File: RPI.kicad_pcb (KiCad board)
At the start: 2 copper layers, 65 x 56 mm, 35 parts, among them J1 Conn_01x02_Male, J2 GPIO, J5 Conn_01x06, J6 Conn_01x04, J7 Conn_01x03, J8 Conn_01x02, J9 Conn_01x02, Q1 IRF9540N, Q2 IRF9540N, Q3 BC856BDW1, SW1 SW_SPDT, SW2 SW_SPDT, U1 LM1085-ADJ

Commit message: Finalised for a check-up
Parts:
- added G***: LOGO, LOGO, F.Cu at (105.3, 85.7)

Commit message: Gerber files generated?
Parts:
- renumbered G*** to G
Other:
- board text removed: "F1"
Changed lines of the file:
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@@
   (net 6 "Net-(D2-Pad1)")
   (net 7 "VD")
-  (net 8 "Net-(J1-Pad2)")
+  (net 8 "Net-(F1-Pad1)")
   (net 9 "/GPIO2{slash}SDA1")
   (net 10 "/GPIO3{slash}SCL1")
@@
     (at 124 96.185263)
     (attr board_only exclude_from_pos_files exclude_from_bom)
-    (fp_text reference "G***" (at 2.182281 1.899801) (layer "F.SilkS")
+    (fp_text reference "G" (at 2.182281 2.814737) (layer "F.SilkS") hide
       (effects (font (size 0.3 0.3) (thickness 0.01)))
     )
@@
       (effects (font (size 1 1) (thickness 0.15)))
     )
-    (fp_text value "10u" (at 1.233747 1.783092 180) (layer "F.Fab")
+    (fp_text value "10u" (at 1.25 -3.516722 180) (layer "F.Fab")
       (effects (font (size 1 1) (thickness 0.15)))
     )
@@
     (property "Value_1" "MCCQ-122")
     (attr through_hole)
-    (fp_text reference "F1" (at 5.7 0.4 90) (layer "F.SilkS")
-      (effects (font (size 1.27 1.27) (thickness 0.254)))
+    (fp_text reference "F1" (at -2.833513 -0.019887 180) (layer "F.SilkS")
+      (effects (font (size 1 1) (thickness 0.15)))
     )
     (fp_text value "MCCQ-122" (at 5.7 0.4 90) (layer "F.SilkS") hide
       (effects (font (size 1.27 1.27) (thickness 0.254)))
     )
-    (fp_text user "${REFERENCE}" (at 5.7 0.4 90) (layer "F.Fab")
+    (fp_text user "${REFERENCE}" (at -2.618494 1.918593 180) (layer "F.Fab")
       (effects (font (size 1.27 1.27) (thickness 0.254)))
     )
@@
     (fp_line (start -1.65 -2) (end 13.05 -2) (layer "F.Fab") (width 0.2))
     (pad "1" thru_hole circle locked (at 0 0 270) (size 3.5 3.5) (drill 2.5239) (layers *.Cu *.Mask)
-      (net 8 "Net-(J1-Pad2)") (pinfunction "1") (pintype "passive"))
+      (net 8 "Net-(F1-Pad1)") (pinfunction "1") (pintype "passive"))
     (pad "2" thru_hole circle locked (at 3.7 0 270) (size 3.5 3.5) (drill 2.5239) (layers *.Cu *.Mask)
-      (net 8 "Net-(J1-Pad2)") (pinfunction "2") (pintype "passive"))
+      (net 8 "Net-(F1-Pad1)") (pinfunction "2") (pintype "passive"))
     (pad "3" thru_hole circle locked (at 7.7 0 270) (size 3.5 3.5) (drill 2.5239) (layers *.Cu *.Mask)
       (net 47 "Net-(F1-Pad3)") (pinfunction "3") (pintype "passive"))
@@
     (at 105.348613 85.695667)
     (attr board_only exclude_from_pos_files exclude_from_bom)
-    (fp_text reference "G***" (at 16.235225 12.411091) (layer "F.SilkS")
+    (fp_text reference "G" (at 0.258943 5.65) (layer "F.SilkS") hide
       (effects (font (size 0.4 0.4) (thickness 0.05)))
     )
@@
       (net 1 "GND") (pinfunction "Pin_1") (pintype "passive"))
     (pad "2" thru_hole circle (at -5 0 90) (size 3.5 3.5) (drill 1.9) (layers *.Cu *.Mask)
-      (net 8 "Net-(J1-Pad2)") (pinfunction "Pin_2") (pintype "passive"))
+      (net 8 "Net-(F1-Pad1)") (pinfunction "Pin_2") (pintype "passive"))
     (model "${KICAD6_3DMODEL_DIR}/Connector_AMASS.3dshapes/AMASS_XT30PW-M_1x02_P2.50mm_Horizontal.wrl"
       (offset (xyz 0 0 0))
@@
     (at 153.826708 61.588613)
     (attr board_only exclude_from_pos_files exclude_from_bom)
-    (fp_text reference "G***" (at -1.194086 2.150782) (layer "F.SilkS")
+    (fp_text reference "G" (at -1.826708 0.411387) (layer "F.SilkS") hide
       (effects (font (size 0.5 0.5) (thickness 0.1)))
     )
@@
     (effects (font (size 0.4 0.4) (thickness 0.08)))
   )
-  (gr_text "F1" (at 124.107573 76.340246) (layer "F.SilkS")
-    (effects (font (size 1 1) (thickness 0.15)))
-  )
   (gr_text "Motor Control" (at 159.915242 65.995222 90) (layer "F.SilkS")

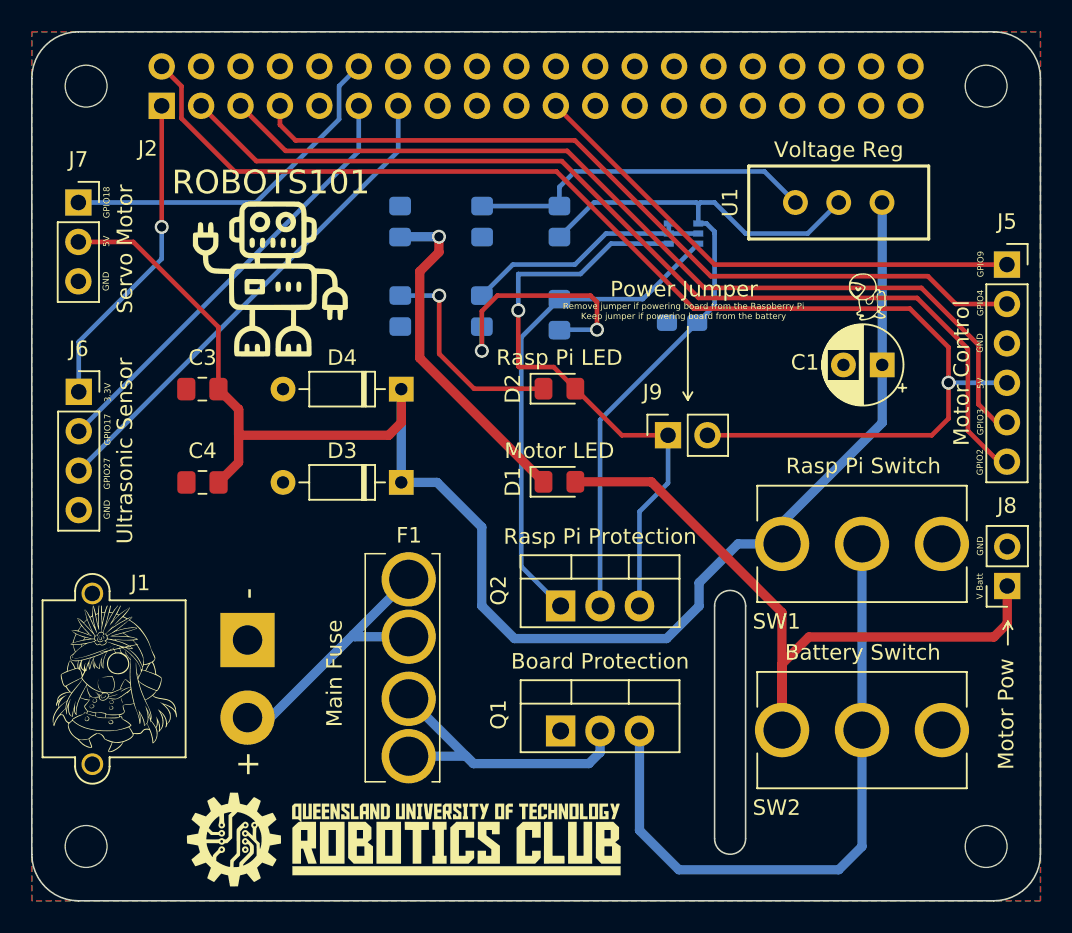
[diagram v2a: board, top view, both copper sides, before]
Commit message: fixed up using Fab ruleset and Matt's input
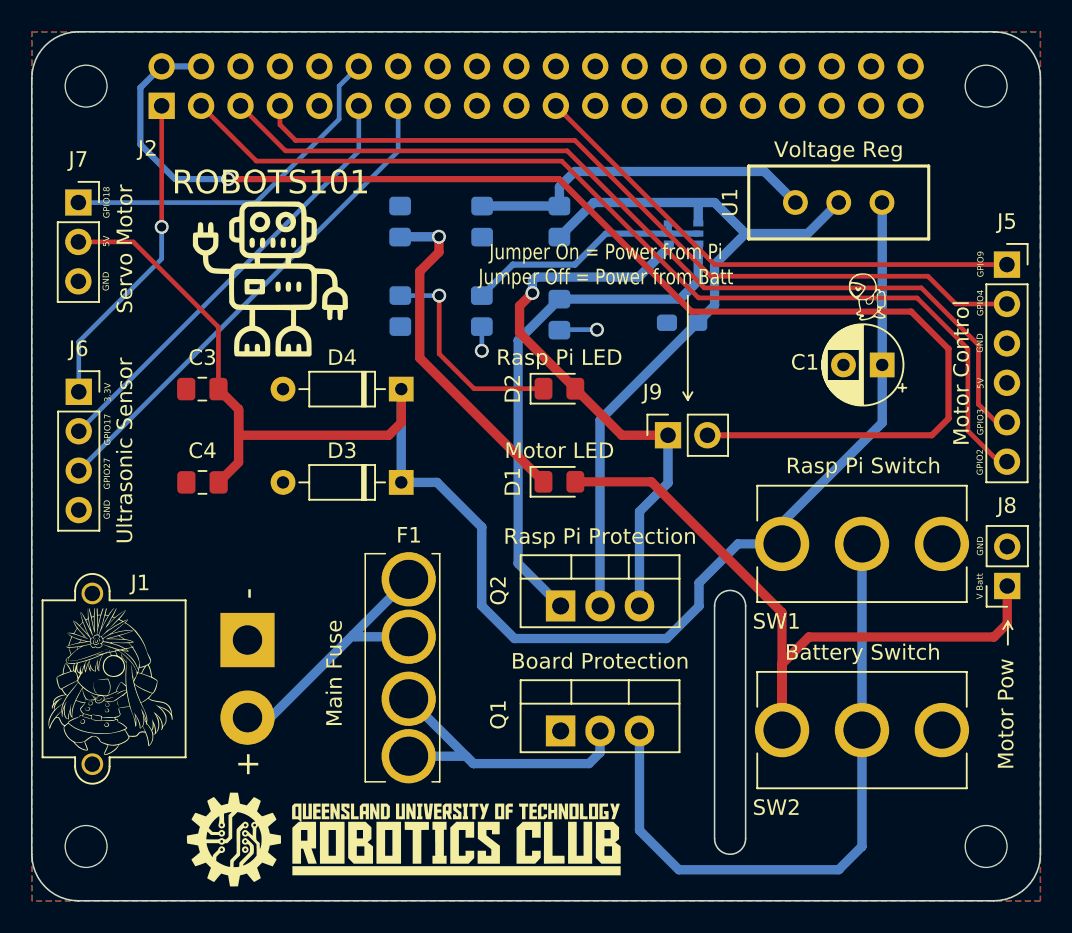
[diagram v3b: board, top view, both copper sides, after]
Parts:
- moved G 0.32 mm to (105.1, 85.9)
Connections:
- J2 pad 4: /5v -> +5V
- J5 pad 4: +5V -> unconnected-(J5-Pad4)
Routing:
- net GND: track 16.3 -> 3.99 mm
- net +5V: track 83.8 -> 86.1 mm
- net VD: track 39.7 -> 37.5 mm
- net Net-(Q2-Pad1): track 32.3 -> 33.6 mm
- net VDDA: track 50.3 -> 49.6 mm
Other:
- board text added: "Jumper On = Power from Pi Jumper Off = Power from Batt"
- board text removed: "Power Jumper"
- board text removed: "Remove jumper if powering board from the Raspberry Pi Keep jumper if powering board from the battery"

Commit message: Added load resistor & updated footprints
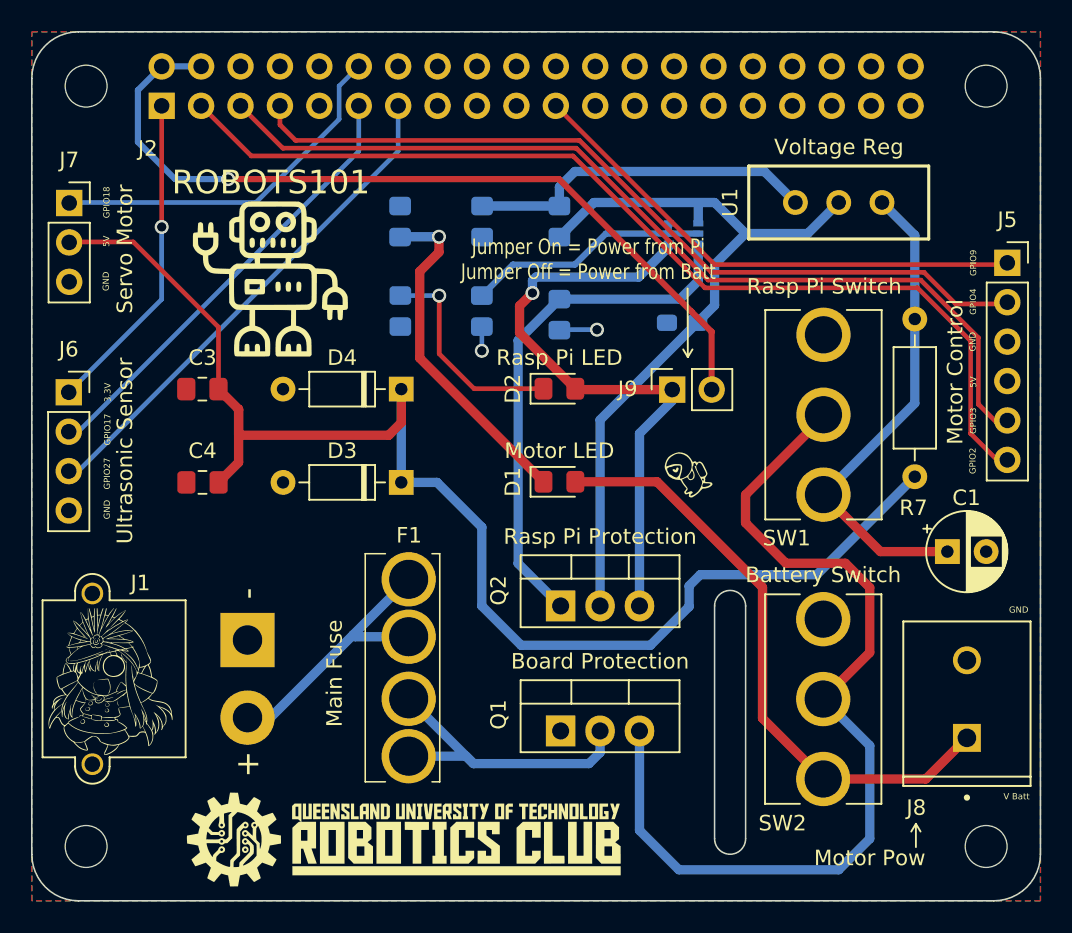
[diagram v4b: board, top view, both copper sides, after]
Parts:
- added R7: 3.3, Resistor_THT:R_Axial_DIN0207_L6.3mm_D2.5mm_P10.16mm_Horizontal, F.Cu at (156.9, 62.5)
- J8: footprint Connector_PinSocket_2.54mm:PinSocket_1x02_P2.54mm_Vertical -> RPi_Hat:TE_282836-2
- moved G 16.1 mm to (142.4, 72.9), turned to 25 degrees
- moved C1 12.7 mm to (159.0, 77.5), turned to 0 degrees
- moved SW1 8.69 mm to (151.0, 68.7), turned to 90 degrees
- moved J8 7.73 mm to (160.3, 87.0), turned to 90 degrees
- moved SW2 3.20 mm to (151.0, 87.0), turned to 90 degrees
- moved J9 2.96 mm to (141.3, 67.1)
- moved J6 0.65 mm to (102.4, 67.2)
- moved J7 0.59 mm to (102.4, 55.0)
- moved J5 0.12 mm to (162.9, 58.9)
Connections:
- C3 pad 1: VCC -> Vdrive
- C4 pad 1: VCC -> Vdrive
- D3 pad 1: VCC -> Vdrive
- D4 pad 1: VCC -> Vdrive
- J7 pad 2: VCC -> Vdrive
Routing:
- net Vdrive: track 0.00 -> 88.8 mm
- net VCC: track 102.8 -> 31.6 mm
- net +5V: track 86.1 -> 53.8 mm
- net Net-(Q1-Pad3): track 41.9 -> 60.6 mm
- net +BATT: track 46.7 -> 39.2 mm
- net VD: track 37.5 -> 39.6 mm
